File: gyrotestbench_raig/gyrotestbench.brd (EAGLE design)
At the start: 160 x 70.8 mm, 81 parts, among them IC3 FT232RL, U1 TESTING_MPU-6050-1, U10 V_REG_LDOSMD, U2 TESTING_MPU-6050-1, U3 TESTING_MPU-6050-1, U8 TESTING_MPU-6050-1, U9 ATMEGA328P, X1 MINI-USB-UX60A-MB-5ST, Y1 8MHz

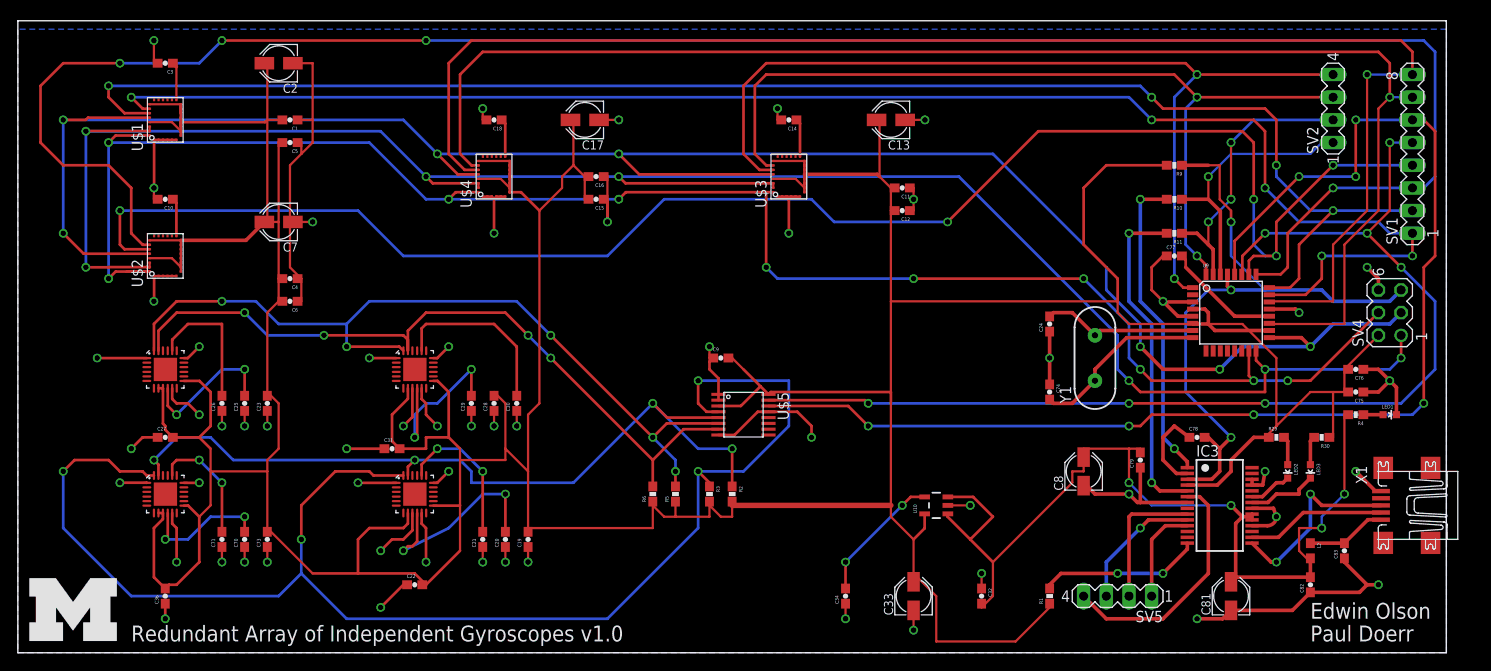
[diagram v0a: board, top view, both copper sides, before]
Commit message: Severed RTS line on FTDI, added pull-ups to LSM chip select lines, and fixed silkscreen font
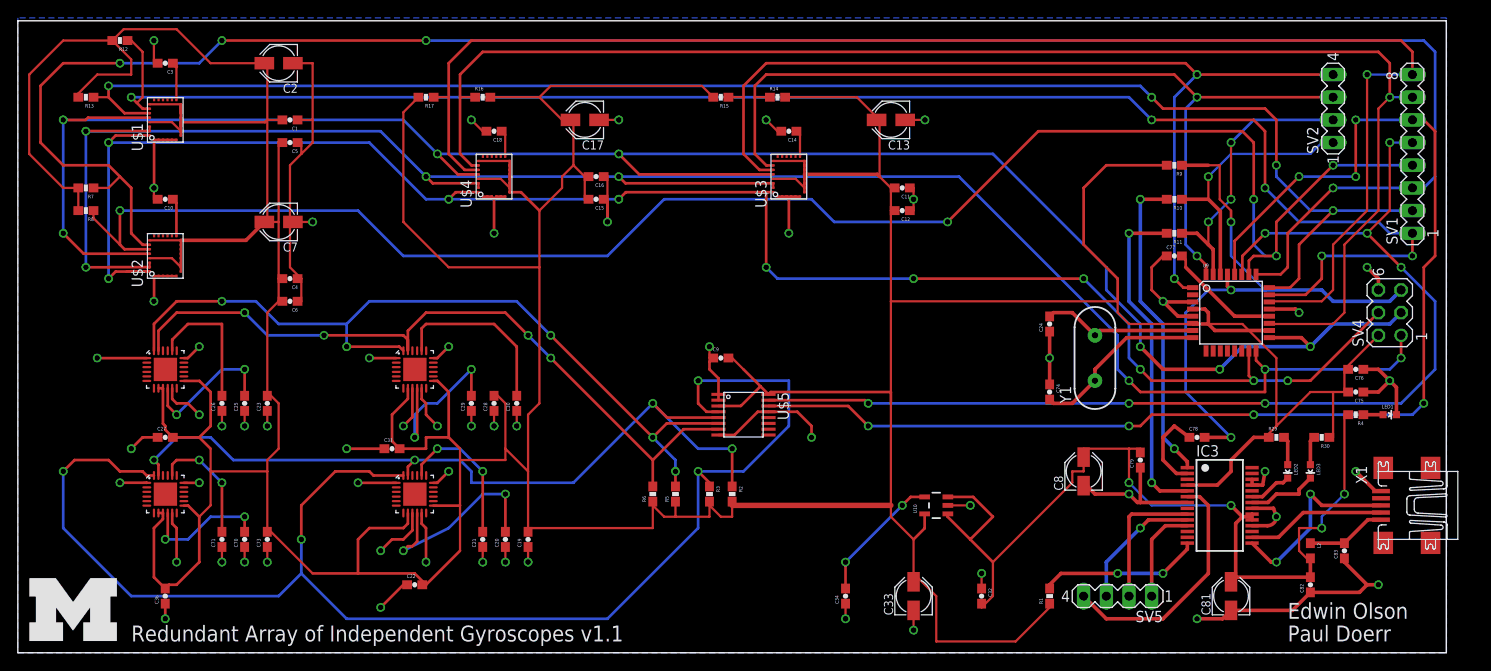
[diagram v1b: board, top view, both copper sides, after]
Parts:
- added R12, R13, R14, R15, R16, R17, R7, R8: 100k, SparkFun-Resistors:0603-RES
- moved C14 1.27 mm to (86.4, 58.4)
- moved C18 1.27 mm to (53.3, 58.4)
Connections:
- net !CS_A0: now also R13.1
- net !CS_A1: now also R8.1
- net !CS_A2: now also R17.1
- net !CS_A3: now also R15.1
- net !CS_G0: now also R12.1
- net !CS_G1: now also R7.1
- net !CS_G2: now also R16.1
- net !CS_G3: now also R14.1
- net 3.3V: now also R12.2, R13.2, R14.2, R15.2, R16.2, R17.2, R7.2, R8.2
- net RESET: no longer IC3.3
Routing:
- net 3.3V: track 634.4 -> 768.9 mm
- net !CS_G0: track 178.0 -> 186.2 mm
- net RESET: track 75.1 -> 67.5 mm
- net !CS_A1: track 185.9 -> 190.9 mm
- net !CS_G1: track 225.9 -> 229.4 mm
- net !CS_G3: track 97.9 -> 99.6 mm
- net !CS_A3: track 105.7 -> 107.4 mm
- net !CS_A0: track 175.1 -> 176.8 mm
- net N$4: track 4.27 -> 3.00 mm
- net N$3: track 4.27 -> 3.00 mm
- net GND: track 300.4 -> 301.5 mm
- net !CS_G2: track 160.4 -> 161.4 mm
- net !CS_A2: track 166.5 -> 167.4 mm
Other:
- board text added: "Redundant Array of Independent Gyroscopes v1.1"
- board text removed: "Redundant Array of Independent Gyroscopes v1.0"

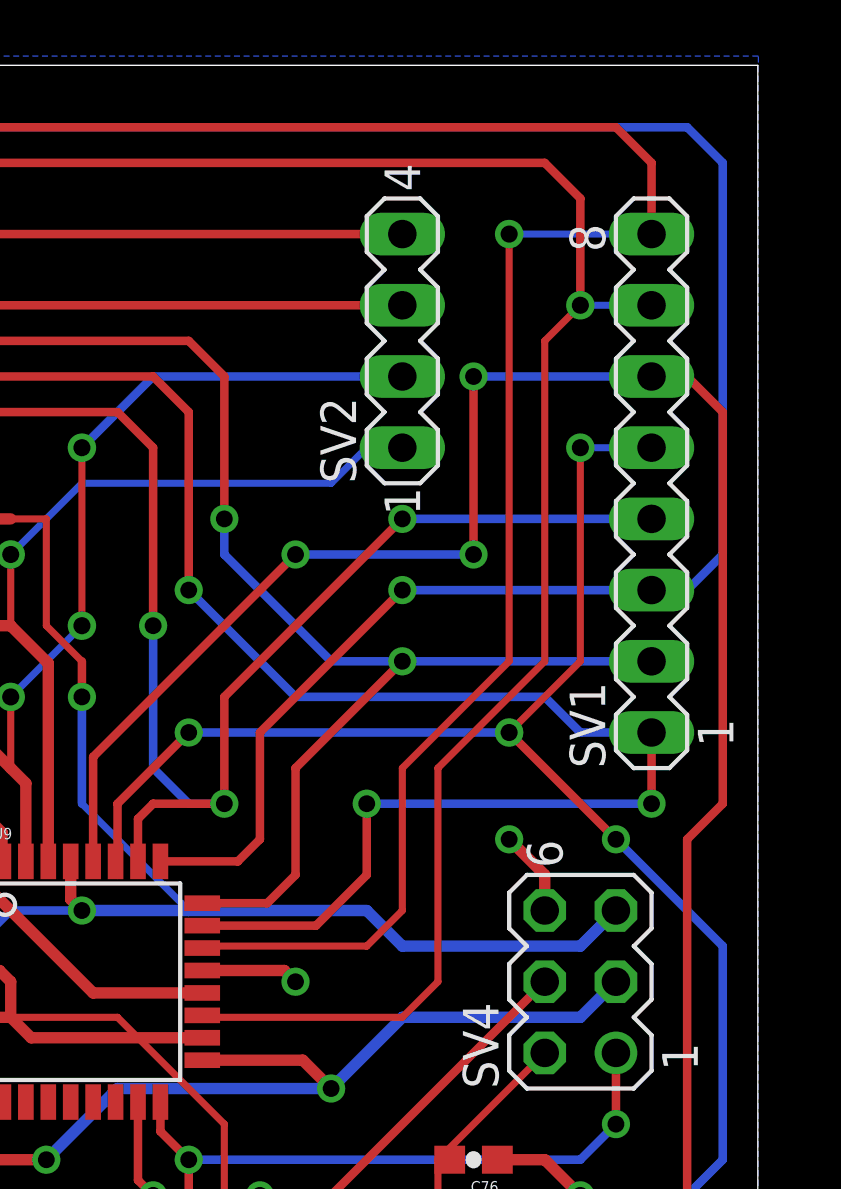
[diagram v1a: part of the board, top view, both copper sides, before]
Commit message: Fixed interface problems, working on first stage IMU processing code
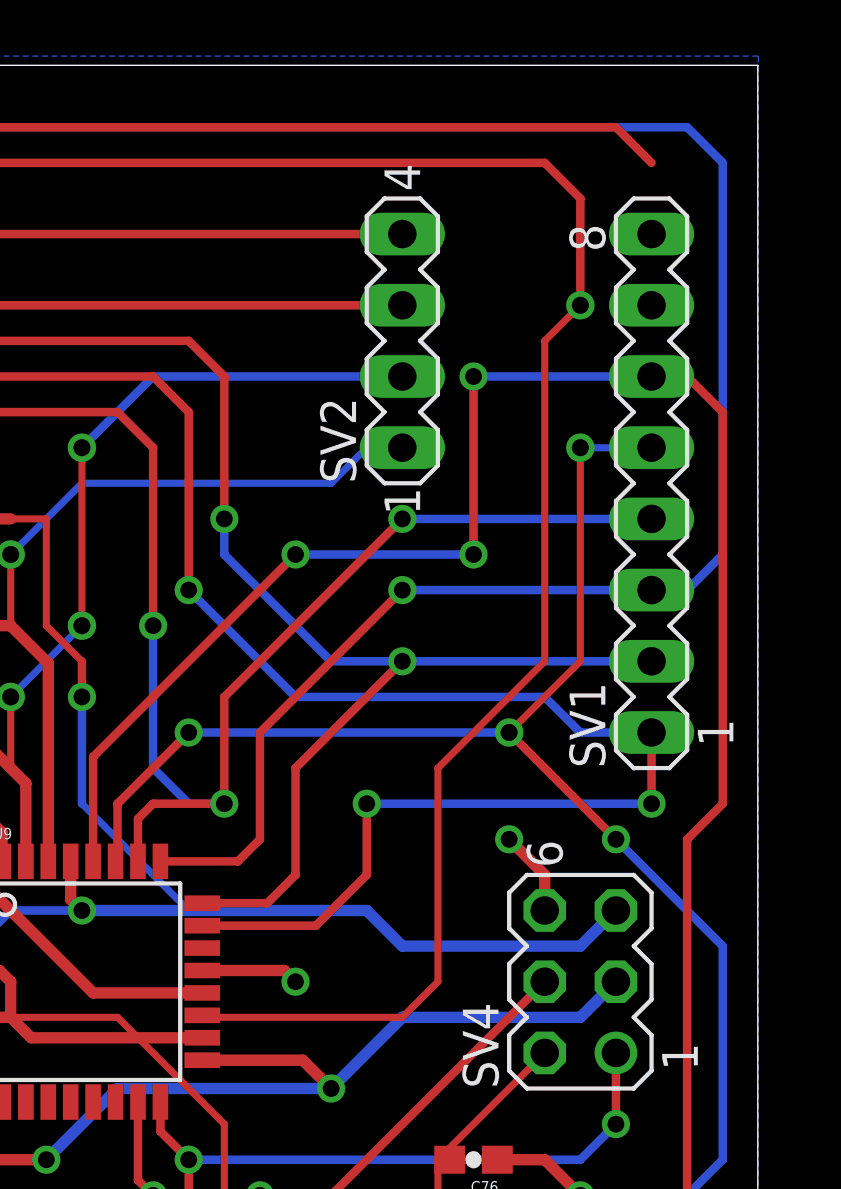
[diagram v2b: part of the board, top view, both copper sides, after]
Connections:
- new net N$16: SV1.7, U9.19
- new net N$17: SV1.8, U9.22
- net !CS_A2: now also U9.13; no longer SV1.8, U9.22
- net !CS_G2: now also U9.12; no longer SV1.7, U9.19
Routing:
- net !CS_A2: track 167.4 -> 125.4 mm, vias 1 -> 0
- net !CS_G2: track 161.4 -> 158.4 mm
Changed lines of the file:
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@@
 <signal name="!CS_G2">
 <contactref element="U$4" pad="P$22"/>
-<contactref element="SV1" pad="7"/>
-<contactref element="U9" pad="19"/>
 <wire x1="152.4" y1="49.53" x2="148.59" y2="45.72" width="0.254" layer="1"/>
 <wire x1="152.4" y1="60.96" x2="152.4" y2="49.53" width="0.254" layer="1"/>
 <wire x1="153.67" y1="62.23" x2="152.4" y2="60.96" width="0.254" layer="1"/>
-<wire x1="156.21" y1="62.23" x2="153.67" y2="62.23" width="0.254" layer="16"/>
-<wire x1="139.7" y1="36.83" x2="140.1826" y2="36.9" width="0.254" layer="1"/>
 <via x="153.67" y="62.23" extent="1-16" drill="0.6096"/>
 <wire x1="51.59" y1="54.59" x2="50.82" y2="54.59" width="0.3048" layer="1"/>
@@
 <wire x1="148.59" y1="38.1" x2="148.59" y2="45.72" width="0.254" layer="1"/>
 <wire x1="51.22" y1="62.23" x2="49.53" y2="62.23" width="0.254" layer="1"/>
+<contactref element="U9" pad="12"/>
+<wire x1="139.7" y1="36.83" x2="135.49" y2="33.8074" width="0" layer="19" extent="1-1"/>
 </signal>
 <signal name="!CS_A2">
 <contactref element="U$4" pad="P$23"/>
-<contactref element="U9" pad="22"/>
-<contactref element="SV1" pad="8"/>
-<wire x1="151.13" y1="49.53" x2="147.32" y2="45.72" width="0.254" layer="1"/>
-<wire x1="151.13" y1="64.77" x2="151.13" y2="49.53" width="0.254" layer="1"/>
-<wire x1="156.21" y1="64.77" x2="151.13" y2="64.77" width="0.254" layer="16"/>
-<wire x1="139.7" y1="39.37" x2="140.1826" y2="39.3" width="0.254" layer="1"/>
-<via x="151.13" y="64.77" extent="1-16" drill="0.6096"/>
 <wire x1="51.59" y1="54.09" x2="50.05" y2="54.09" width="0.3048" layer="1"/>
 <wire x1="50.05" y1="54.09" x2="48.26" y2="55.88" width="0.3048" layer="1"/>
@@
 <wire x1="50.8" y1="68.58" x2="154.94" y2="68.58" width="0.3048" layer="1"/>
 <wire x1="154.94" y1="68.58" x2="156.21" y2="67.31" width="0.3048" layer="1"/>
-<wire x1="156.21" y1="67.31" x2="156.21" y2="64.77" width="0.3048" layer="1"/>
 <contactref element="R17" pad="1"/>
-<wire x1="139.7" y1="39.37" x2="146.05" y2="39.37" width="0.254" layer="1"/>
-<wire x1="146.05" y1="39.37" x2="147.32" y2="40.64" width="0.254" layer="1"/>
-<wire x1="147.32" y1="40.64" x2="147.32" y2="45.72" width="0.254" layer="1"/>
 <wire x1="46.57" y1="62.23" x2="48.26" y2="62.23" width="0.254" layer="1"/>
+<contactref element="U9" pad="13"/>
+<wire x1="156.21" y1="67.31" x2="136.29" y2="33.8074" width="0" layer="19" extent="1-1"/>
 </signal>
 <signal name="SCL">
@@
 <wire x1="138.245" y1="12.935" x2="141.205" y2="12.935" width="0.4064" layer="1"/>
 </signal>
+<signal name="N$16">
+<contactref element="U9" pad="19"/>
+<contactref element="SV1" pad="7"/>
+<wire x1="140.1826" y1="36.9" x2="156.21" y2="62.23" width="0" layer="19" extent="1-1"/>
+</signal>
+<signal name="N$17">
+<contactref element="U9" pad="22"/>
+<contactref element="SV1" pad="8"/>
+<wire x1="140.1826" y1="39.3" x2="156.21" y2="64.77" width="0" layer="19" extent="1-1"/>
+</signal>
 </signals>
